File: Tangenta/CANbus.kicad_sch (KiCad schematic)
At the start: 1 part

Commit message: Removing component association with previous project (local) libraries.
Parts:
- C105: footprint CholaFootprintsPrjLib:CAP_L5 -> CAP_L5:CAP_L5; symbol CholaSymbolsPrjLib:16CE47FSS -> 16CE47FSS:16CE47FSS
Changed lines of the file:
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@@
 	)
 	(symbol
-		(lib_id "CholaSymbolsPrjLib:16CE47FSS")
+		(lib_id "16CE47FSS:16CE47FSS")
 		(at 46.99 36.83 0)
 		(unit 1)
@@
 			)
 		)
-		(property "Footprint" "CholaFootprintsPrjLib:CAP_L5"
+		(property "Footprint" "CAP_L5:CAP_L5"
 			(at 45.72 54.61 0)
 			(effects

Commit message: Fixes, before checks.
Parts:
- C105: symbol 16CE47FSS:16CE47FSS -> CAP_L5:16CE47FSS
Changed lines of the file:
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@@
 	)
 	(symbol
-		(lib_id "16CE47FSS:16CE47FSS")
+		(lib_id "CAP_L5:16CE47FSS")
 		(at 46.99 36.83 0)
 		(unit 1)

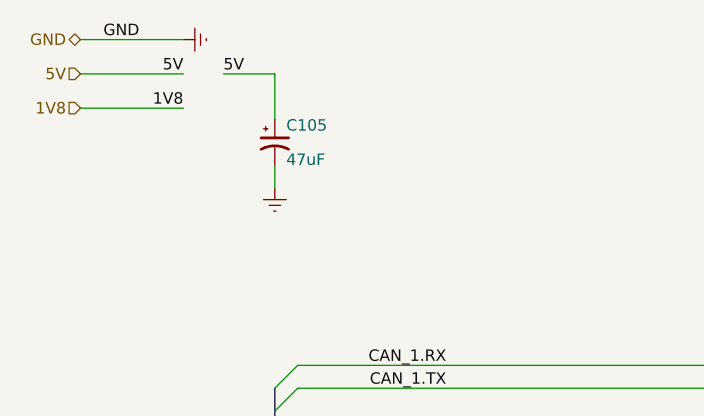
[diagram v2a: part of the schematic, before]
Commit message: Reverting to the original design.
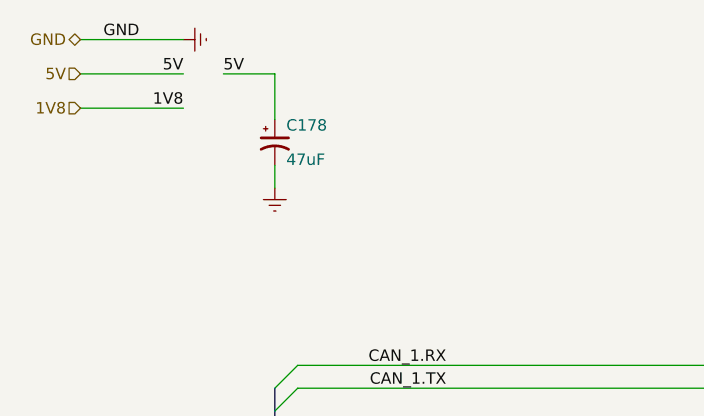
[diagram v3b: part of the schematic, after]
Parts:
- C178: renamed from C105; symbol CAP_L5:16CE47FSS -> CholaSymbolsPrjLib:16CE47FSS

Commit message: initialize branch
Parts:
- renumbered C178 to C105
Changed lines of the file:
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@@
   (symbol (lib_id "CholaSymbolsPrjLib:16CE47FSS") (at 46.99 36.83 0) (unit 1)
     (in_bom yes) (on_board yes) (dnp no)
-    (property "Reference" "C178" (at 48.26 34.925 0)
+    (property "Reference" "C105" (at 48.26 34.925 0)
       (effects (font (size 1.27 1.27)) (justify left))
     )
@@
     (instances
       (project "Tangenta"
-        (path "/358d1bcf-7599-4352-8c4d-baa18a5f09e6/2bb52479-7b35-496d-9807-27e706c6ef7b/c653b84e-94ee-4be9-b47c-8c767f88973e"
-          (reference "C178") (unit 1)
-        )
-        (path "/358d1bcf-7599-4352-8c4d-baa18a5f09e6/98e3b24f-9927-4339-b8fd-9deea91a522a"
-          (reference "C184") (unit 1)
-        )
         (path "/358d1bcf-7599-4352-8c4d-baa18a5f09e6/b5394a48-5ef8-44c9-9d56-604d4ce6d7c8"
           (reference "C105") (unit 1)
@@
   (symbol (lib_id "power:GNDREF") (at 46.99 41.91 0) (unit 1)
     (in_bom yes) (on_board yes) (dnp no) (fields_autoplaced)
-    (property "Reference" "#PWR030" (at 46.99 48.26 0)
+    (property "Reference" "#PWR060" (at 46.99 48.26 0)
       (effects (font (size 1.27 1.27)) hide)
     )
@@
     (instances
       (project "Tangenta"
-        (path "/358d1bcf-7599-4352-8c4d-baa18a5f09e6/b1871a4d-6a35-44e2-a9a2-9a4af684371d"
-          (reference "#PWR030") (unit 1)
-        )
-        (path "/358d1bcf-7599-4352-8c4d-baa18a5f09e6/f1c5822c-e7b8-40ae-bab0-71fd1c2cfc7c"
-          (reference "#PWR035") (unit 1)
-        )
-        (path "/358d1bcf-7599-4352-8c4d-baa18a5f09e6/98e3b24f-9927-4339-b8fd-9deea91a522a"
-          (reference "#PWR081") (unit 1)
-        )
         (path "/358d1bcf-7599-4352-8c4d-baa18a5f09e6/b5394a48-5ef8-44c9-9d56-604d4ce6d7c8"
           (reference "#PWR060") (unit 1)
@@
   (symbol (lib_id "power:GNDREF") (at 36.83 25.4 90) (unit 1)
     (in_bom yes) (on_board yes) (dnp no) (fields_autoplaced)
-    (property "Reference" "#PWR030" (at 43.18 25.4 0)
+    (property "Reference" "#PWR059" (at 43.18 25.4 0)
       (effects (font (size 1.27 1.27)) hide)
     )
@@
     (instances
       (project "Tangenta"
-        (path "/358d1bcf-7599-4352-8c4d-baa18a5f09e6/b1871a4d-6a35-44e2-a9a2-9a4af684371d"
-          (reference "#PWR030") (unit 1)
-        )
-        (path "/358d1bcf-7599-4352-8c4d-baa18a5f09e6/f1c5822c-e7b8-40ae-bab0-71fd1c2cfc7c"
-          (reference "#PWR035") (unit 1)
-        )
-        (path "/358d1bcf-7599-4352-8c4d-baa18a5f09e6/98e3b24f-9927-4339-b8fd-9deea91a522a"
-          (reference "#PWR076") (unit 1)
-        )
         (path "/358d1bcf-7599-4352-8c4d-baa18a5f09e6/b5394a48-5ef8-44c9-9d56-604d4ce6d7c8"
           (reference "#PWR059") (unit 1)

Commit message: CAP_L5, CR2032_HOL, Ferrite_Bead, XTAL_24-25
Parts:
- C105: footprint CAP_L5:CAP_L5 -> CholaFootprintsPrjLib:CAP_L5
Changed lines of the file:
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@@
       (effects (font (size 1.27 1.27)) (justify left))
     )
-    (property "Footprint" "CAP_L5:CAP_L5" (at 45.72 54.61 0)
+    (property "Footprint" "CholaFootprintsPrjLib:CAP_L5" (at 45.72 54.61 0)
       (effects (font (size 1.27 1.27) italic) hide)
     )
